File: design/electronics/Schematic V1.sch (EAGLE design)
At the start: 182 parts, among them J1 PJ-202AH, J3 DD50P564GTXLF, J4 DD50P564GTXLF

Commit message: Added Traces
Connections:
- net S_GND: now also STM32F2B.BOOT0
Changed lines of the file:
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@@
 <label x="88.9" y="81.28" size="1.778" layer="95"/>
+</segment>
+<segment>
+<pinref part="STM32F2" gate="B" pin="BOOT0"/>
+<wire x1="93.98" y1="190.5" x2="99.06" y2="190.5" width="0.1524" layer="91"/>
+<label x="96.52" y="190.5" size="1.778" layer="95"/>
 </segment>
 </net>

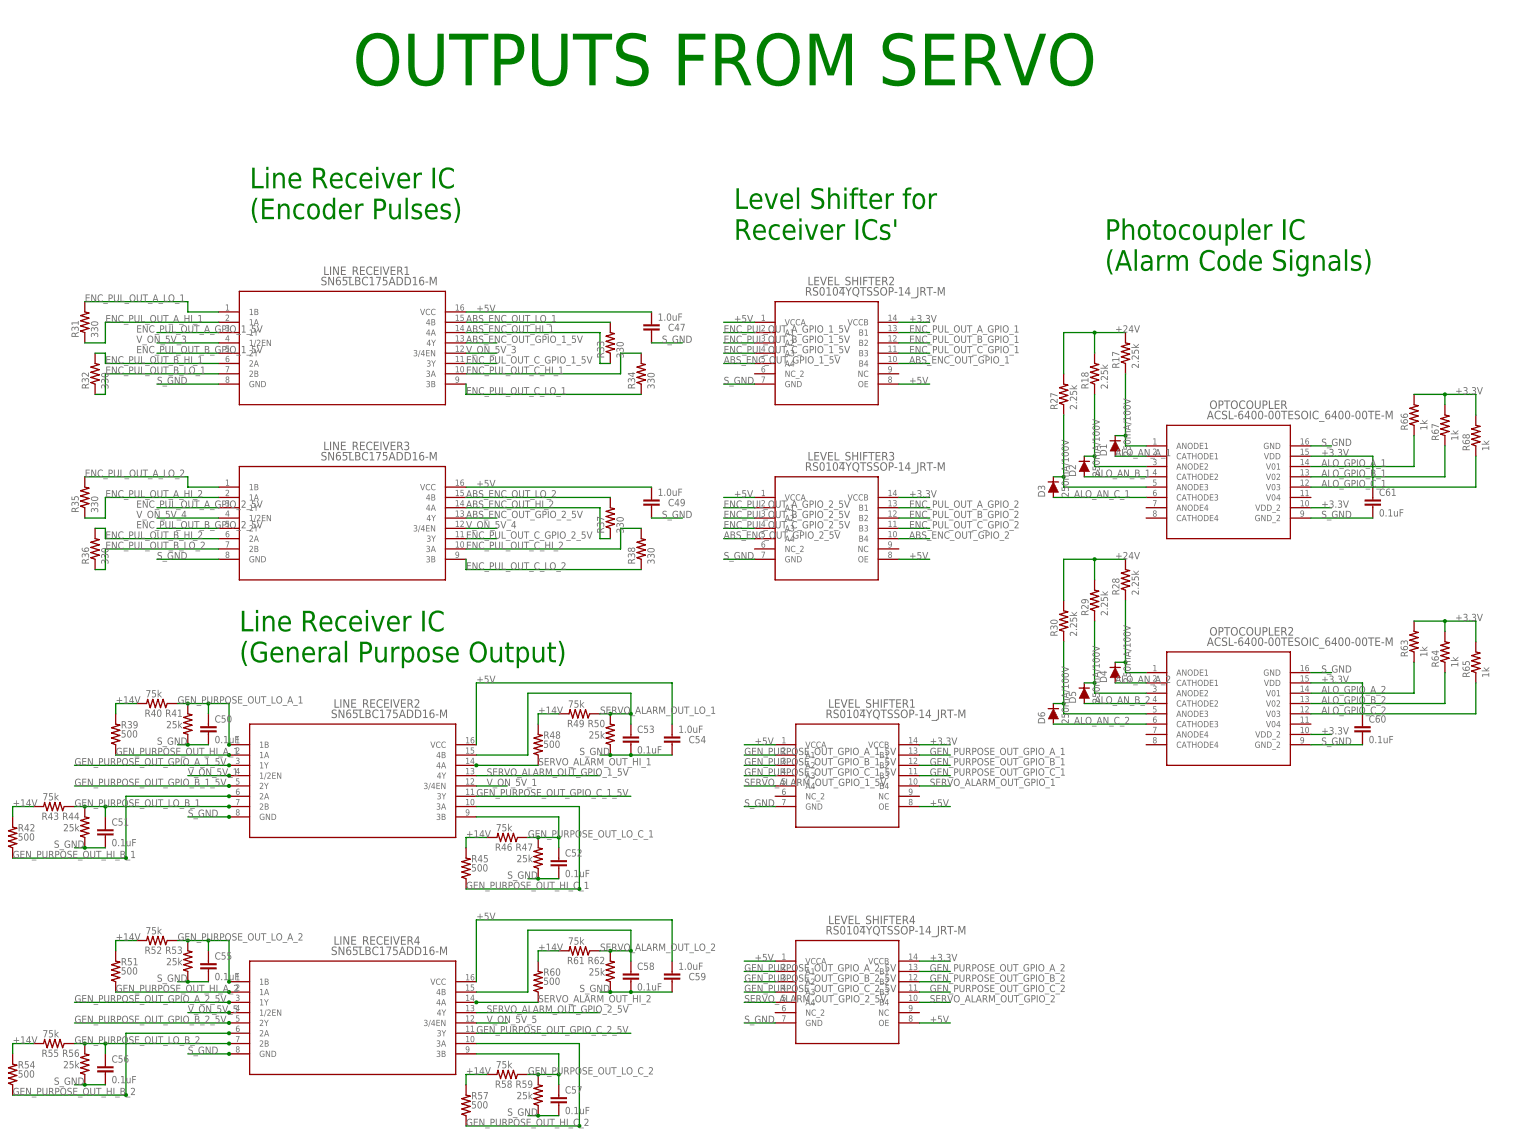
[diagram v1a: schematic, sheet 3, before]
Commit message: Added jumper connectors to DAC input, added EXT IO Pins
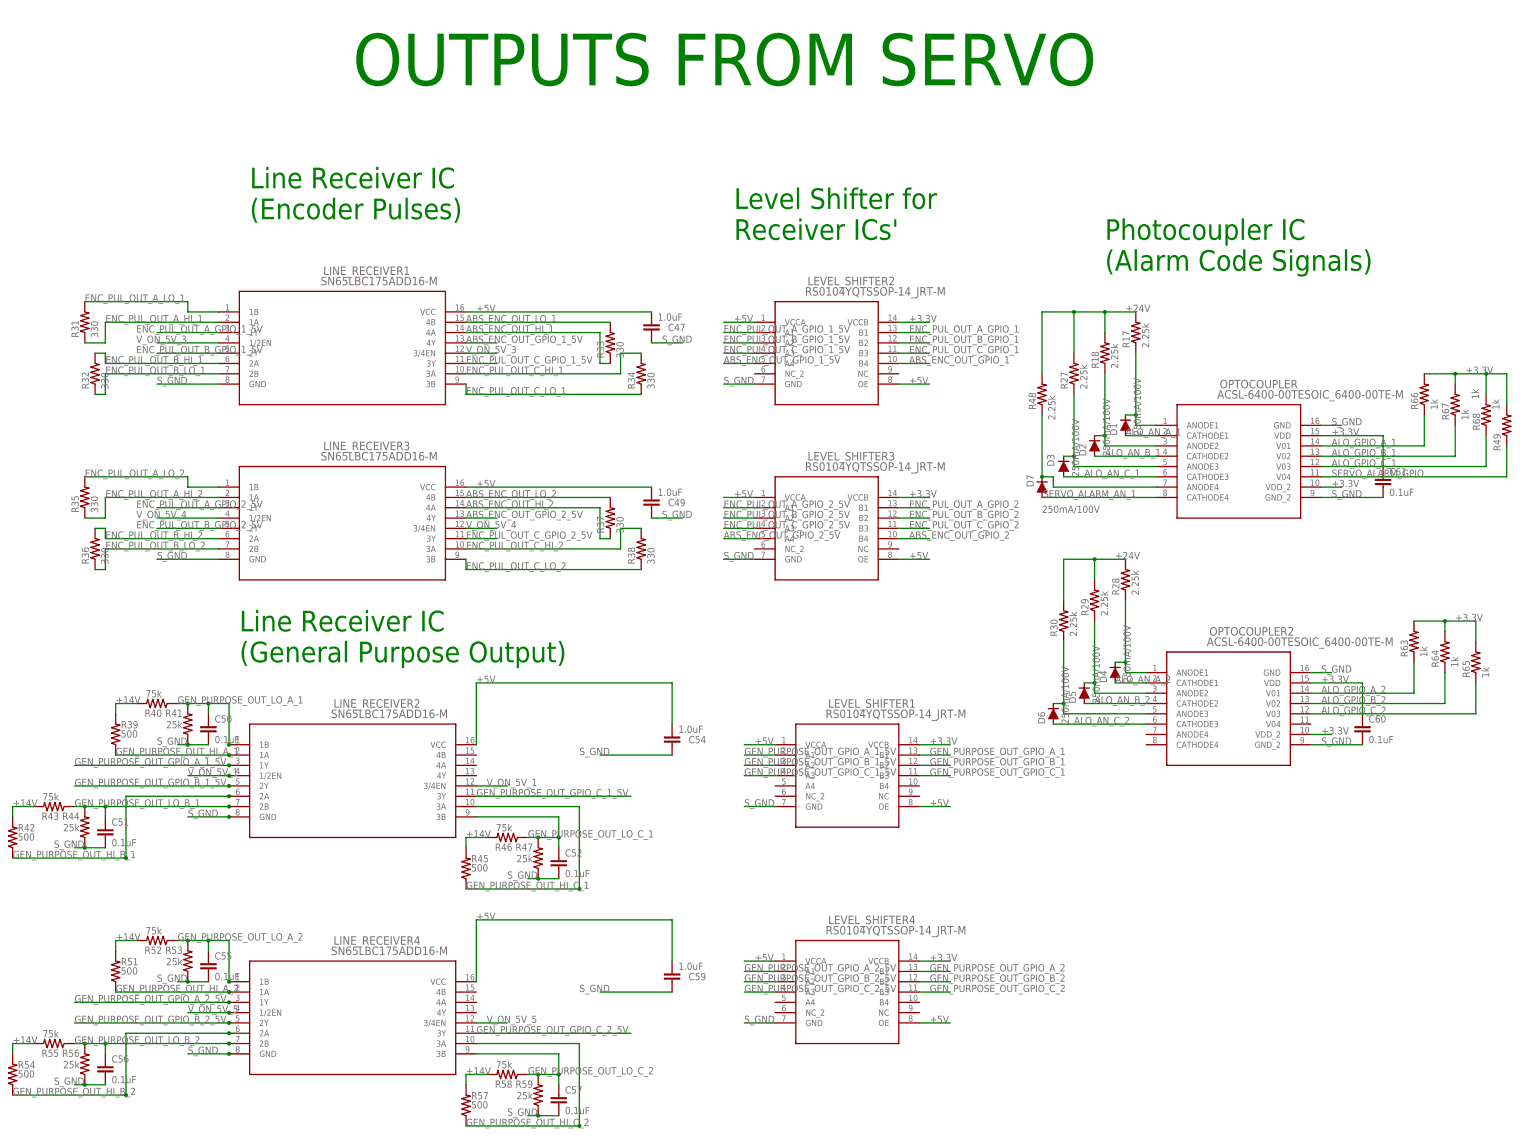
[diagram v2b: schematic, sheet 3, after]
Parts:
- removed C53, C58: 0.1uF, SparkFun-Capacitors:1.0UF-0805-25V-10%
- removed R50, R62: 25k, rcl:R-US_R0805
- removed R60: 500, rcl:R-US_R0805
- removed R61: 75k, rcl:R-US_R0805
- added D7: 250mA/100V, SparkFun-DiscreteSemi:DIODE-BAS16J
- added J2, J5: TSM-103-01-L-SVJ, SSW-130-01-G-S:TSM-103-01-L-SVJ
- R48: value 500 -> 2.25k
- R49: value 75k -> 1k
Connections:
- removed net N$12: OP_AMP.+IN_1, R7.2
- removed net SERVO_ALARM_OUT_GPIO_1: LEVEL_SHIFTER1.B4, STM32F2A.PB11
- removed net SERVO_ALARM_OUT_GPIO_1_5V: LEVEL_SHIFTER1.A4, LINE_RECEIVER2.4Y
- removed net SERVO_ALARM_OUT_GPIO_2: LEVEL_SHIFTER4.B4, STM32F2A.PB8
- removed net SERVO_ALARM_OUT_GPIO_2_5V: LEVEL_SHIFTER4.A4, LINE_RECEIVER4.4Y
- removed net SERVO_ALARM_OUT_HI_1: J3.31, LINE_RECEIVER2.4A, R48.1
- removed net SERVO_ALARM_OUT_HI_2: J4.31, LINE_RECEIVER4.4A, R60.1
- removed net SERVO_ALARM_OUT_LO_1: C53.2, J3.32, LINE_RECEIVER2.4B, R49.1, R50.2
- removed net SERVO_ALARM_OUT_LO_2: C58.2, J4.32, LINE_RECEIVER4.4B, R61.1, R62.2
- new net 1.65V: J2.3, J5.3, OP_AMP.+IN_1, R7.2
- new net DAC_1_IN: J2.2, R11.1
- new net DAC_2_IN: J5.2, R16.1
- new net EXT_IO1: STM32F2A.PB12
- new net EXT_IO10: STM32F2A.PA8
- new net EXT_IO11: STM32F2A.PA9
- new net EXT_IO2: STM32F2A.PB13
- new net EXT_IO3: STM32F2A.PD10
- new net EXT_IO4: STM32F2A.PD11
- new net EXT_IO5: STM32F2A.PD13
- new net EXT_IO6: STM32F2A.PD14
- new net EXT_IO7: STM32F2A.PD15
- new net EXT_IO8: STM32F2A.PC8
- new net EXT_IO9: STM32F2A.PC9
- new net N$6: D7.C, OPTOCOUPLER.ANODE4, R48.1
- new net SERVO_ALARM_AN_1: D7.A, J3.31, OPTOCOUPLER.CATHODE4
- new net SERVO_ALARM_AN_2: J3.32, J4.31
- new net SERVO_ALARM_GPIO: OPTOCOUPLER.V04, R49.1, STM32F2A.PA2
- net +14V: no longer R48.2, R49.2, R60.2, R61.2
- net +24V: now also R48.2
- net +3.3V: now also R49.2
- net ABS_ENC_OUT_GPIO_1: now also STM32F2B.PE14; no longer STM32F2B.PE13
- net ABS_ENC_OUT_GPIO_2: now also STM32F2A.PB6; no longer STM32F2A.PB4
- net CLR_GPIO_1: now also STM32F2A.PD8; no longer STM32F2A.PB15
- net DIR_GPIO_1: now also STM32F2A.PB15; no longer STM32F2A.PB14
- net ENC_PUL_OUT_A_GPIO_1: now also STM32F2A.PD12; no longer STM32F2B.PE10
- net ENC_PUL_OUT_A_GPIO_2: now also STM32F2A.PB3; no longer STM32F2A.PD6
- net ENC_PUL_OUT_B_GPIO_2: now also STM32F2A.PB4; no longer STM32F2A.PD7
- net ENC_PUL_OUT_C_GPIO_1: now also STM32F2B.PE13; no longer STM32F2B.PE12
- net ENC_PUL_OUT_C_GPIO_2: now also STM32F2A.PB5; no longer STM32F2A.PB3
- net GEN_PURPOSE_OUT_GPIO_A_1: now also STM32F2B.PE15; no longer STM32F2B.PE14
- net GEN_PURPOSE_OUT_GPIO_A_2: now also STM32F2A.PB7; no longer STM32F2A.PB5
- net GEN_PURPOSE_OUT_GPIO_B_1: now also STM32F2A.PB10; no longer STM32F2B.PE15
- net GEN_PURPOSE_OUT_GPIO_B_2: now also STM32F2A.PB8; no longer STM32F2A.PB6
- net GEN_PURPOSE_OUT_GPIO_C_1: now also STM32F2A.PB11; no longer STM32F2A.PB10
- net GEN_PURPOSE_OUT_GPIO_C_2: now also STM32F2A.PB9; no longer STM32F2A.PB7
- net POS_EN_GPIO: now also STM32F2A.PD9; no longer STM32F2A.PD8
- net PULSE_GPIO_1: now also STM32F2A.PB14; no longer STM32F2A.PB13
- net P_GND: now also J4.32
- net S_GND: no longer C53.1, C58.1, R50.1, R62.1
- net TORQUE-SPEED_DAC_1: now also J2.1; no longer R11.1
- net TORQUE-SPEED_DAC_2: now also J5.1; no longer R16.1
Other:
- note added: "24V Input"
- note added: "DAC Jumpers"
- moved on the sheet: 14_JACK, C61, D1, D2, D3, J1, OPTOCOUPLER, R17, R18, R27, R48, R49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

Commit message: Finished Design
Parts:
- added LED10: INDIC_LED, led:LEDCHIPLED_0805
- added LED5: UART_LED, led:LEDCHIPLED_0805
- added LED6: POS_CON_LED, led:LEDCHIPLED_0805
- added LED7: ALO1, led:LEDCHIPLED_0805
- added LED8: ALO2, led:LEDCHIPLED_0805
- added LED9: ALO3, led:LEDCHIPLED_0805
- added R50, R60, R61, R62, R77, R78: 150, rcl:R-US_R0805
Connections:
- new net ALO1_LED: R61.1, STM32F2B.PE2
- new net ALO2_LED: R62.1, STM32F2B.PE3
- new net ALO3_LED: R77.1, STM32F2B.PE4
- new net INDIC_LED: R78.1, STM32F2B.PE5
- new net N$10: LED6.A, R60.2
- new net N$12: LED7.A, R61.2
- new net N$14: LED8.A, R62.2
- new net N$16: LED9.A, R77.2
- new net N$19: LED10.A, R78.2
- new net N$9: LED5.A, R50.2
- new net POS_CON_LED: R60.1, STM32F2B.PE1
- new net UART_LED: R50.1, STM32F2B.PE0
- net P_GND: now also LED10.C, LED5.C, LED6.C, LED7.C, LED8.C, LED9.C
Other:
- note added: "Signal LEDs"
- note added: "Voltage LEDs"
- note removed: "Test LEDs"
- moved on the sheet: ST-LINK_CONNECTOR, TP1, TP2, TP3, TP4, TP5, TP6

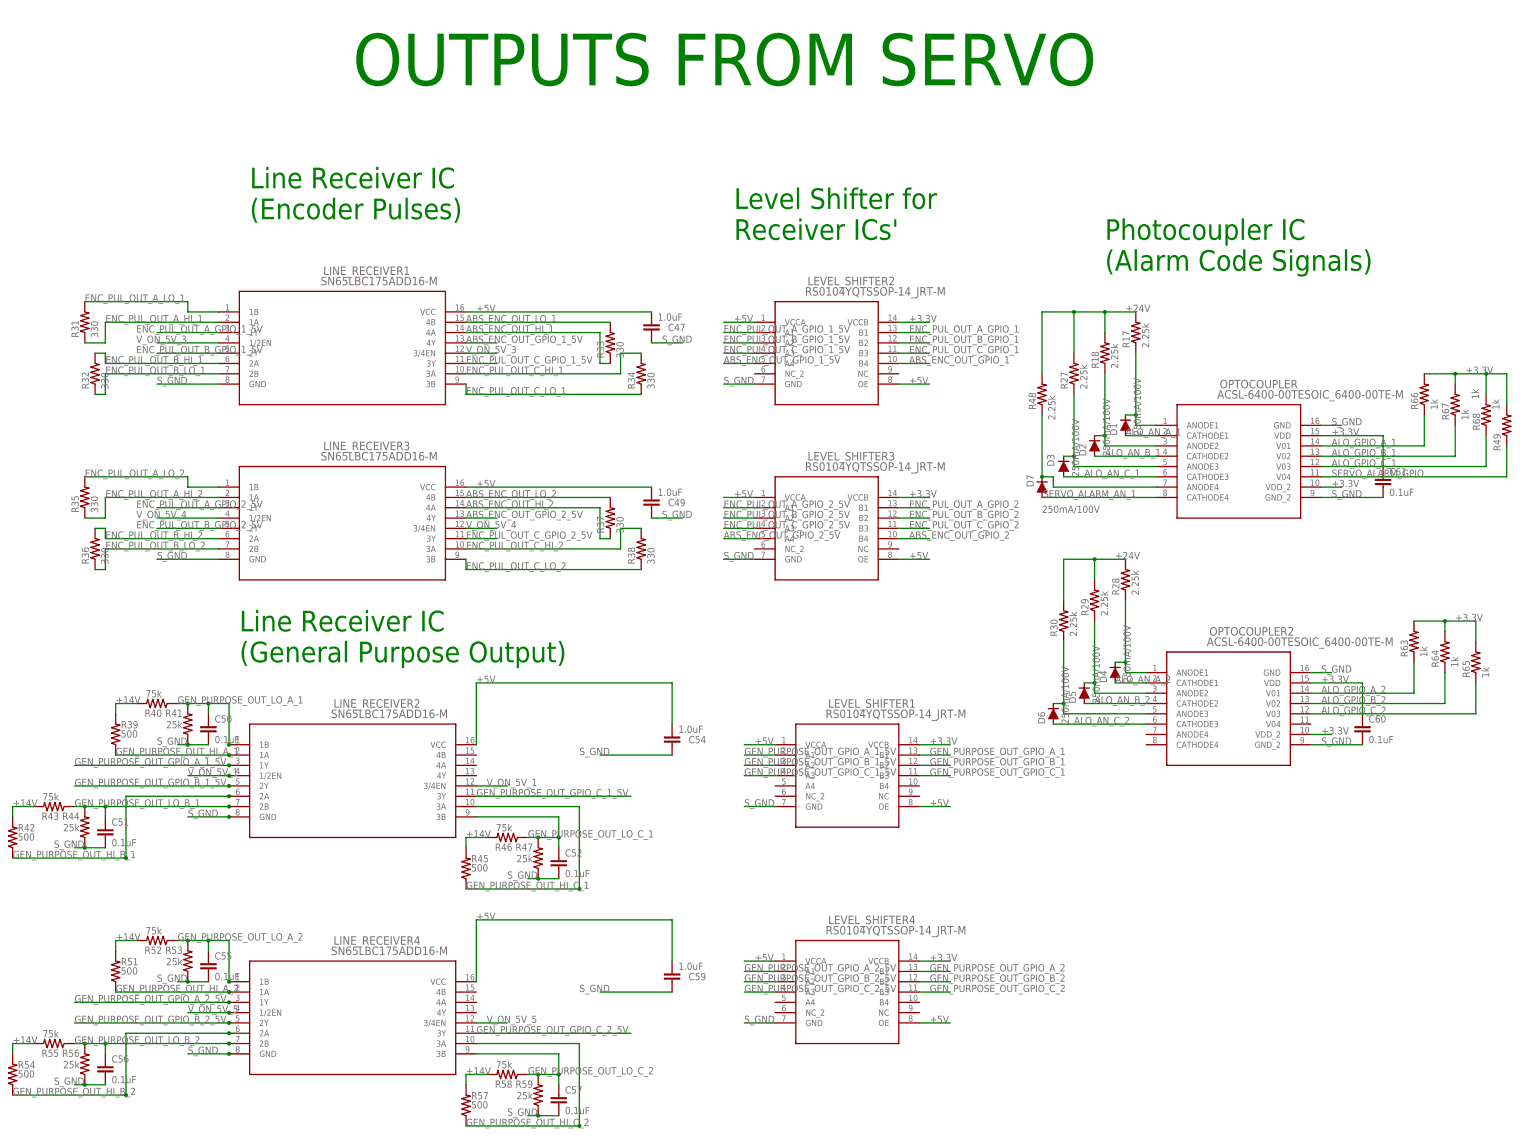
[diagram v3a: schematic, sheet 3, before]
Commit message: Added pull downs to level shifter 5V lines
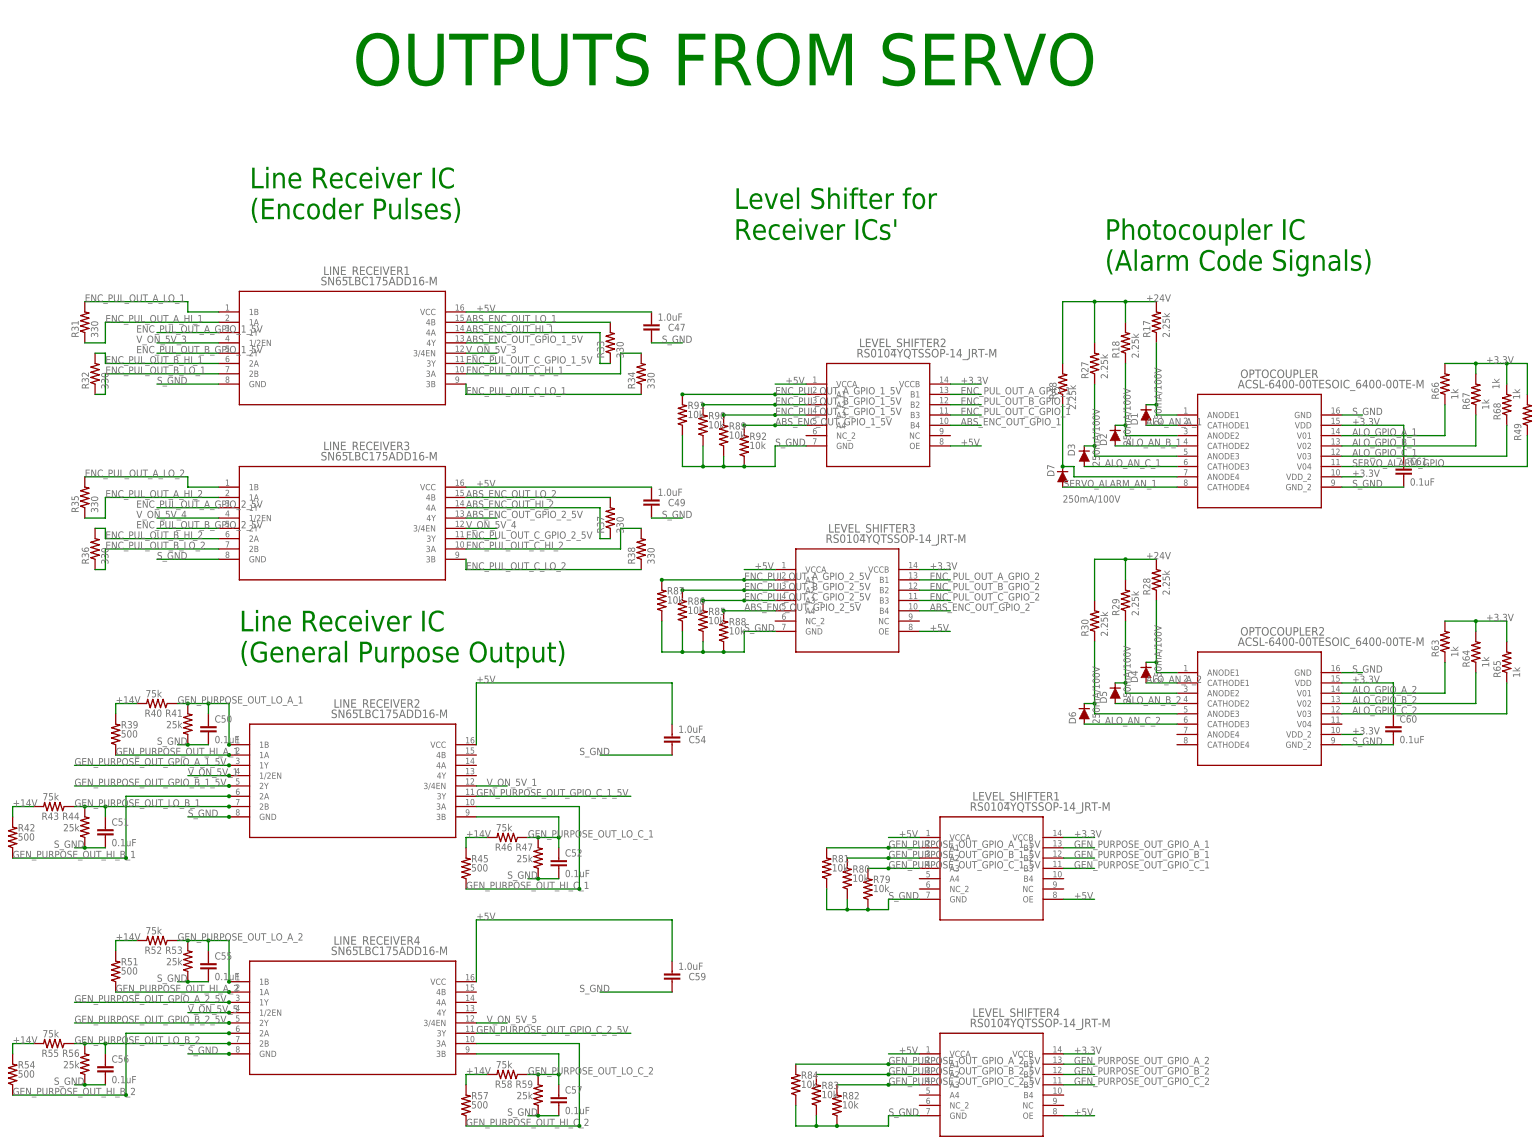
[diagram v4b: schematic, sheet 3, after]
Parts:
- added R79, R80, R81, R82, R83, R84, R85, R86, R87, R88, R89, R90, R91, R92: 10k, rcl:R-US_R0805
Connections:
- net ABS_ENC_OUT_GPIO_1_5V: now also R92.2
- net ABS_ENC_OUT_GPIO_2_5V: now also R88.2
- net ENC_PUL_OUT_A_GPIO_1_5V: now also R91.2
- net ENC_PUL_OUT_A_GPIO_2_5V: now also R87.2
- net ENC_PUL_OUT_B_GPIO_1_5V: now also R90.2
- net ENC_PUL_OUT_B_GPIO_2_5V: now also R86.2
- net ENC_PUL_OUT_C_GPIO_1_5V: now also R89.2
- net ENC_PUL_OUT_C_GPIO_2_5V: now also R85.2
- net GEN_PURPOSE_OUT_GPIO_A_1_5V: now also R81.2
- net GEN_PURPOSE_OUT_GPIO_A_2_5V: now also R84.2
- net GEN_PURPOSE_OUT_GPIO_B_1_5V: now also R80.2
- net GEN_PURPOSE_OUT_GPIO_B_2_5V: now also R83.2
- net GEN_PURPOSE_OUT_GPIO_C_1_5V: now also R79.2
- net GEN_PURPOSE_OUT_GPIO_C_2_5V: now also R82.2
- net S_GND: now also R79.1, R80.1, R81.1, R82.1, R83.1, R84.1, R85.1, R86.1, R87.1, R88.1, R89.1, R90.1, R91.1, R92.1
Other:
- moved on the sheet: C60, C61, D1, D2, D3, D4, D5, D6, D7, LEVEL_SHIFTER1, LEVEL_SHIFTER2, LEVEL_SHIFTER3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
